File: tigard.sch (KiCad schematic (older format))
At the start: 89 parts, among them J1 USB_C_Receptacle_USB2.0, J2 JTAG, J3 UART, J4 SPI, J5 CORTEX, J6 LA, Q1 BSH103, SW1 TARGET, SW2 MODE, U1 AP7365-18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

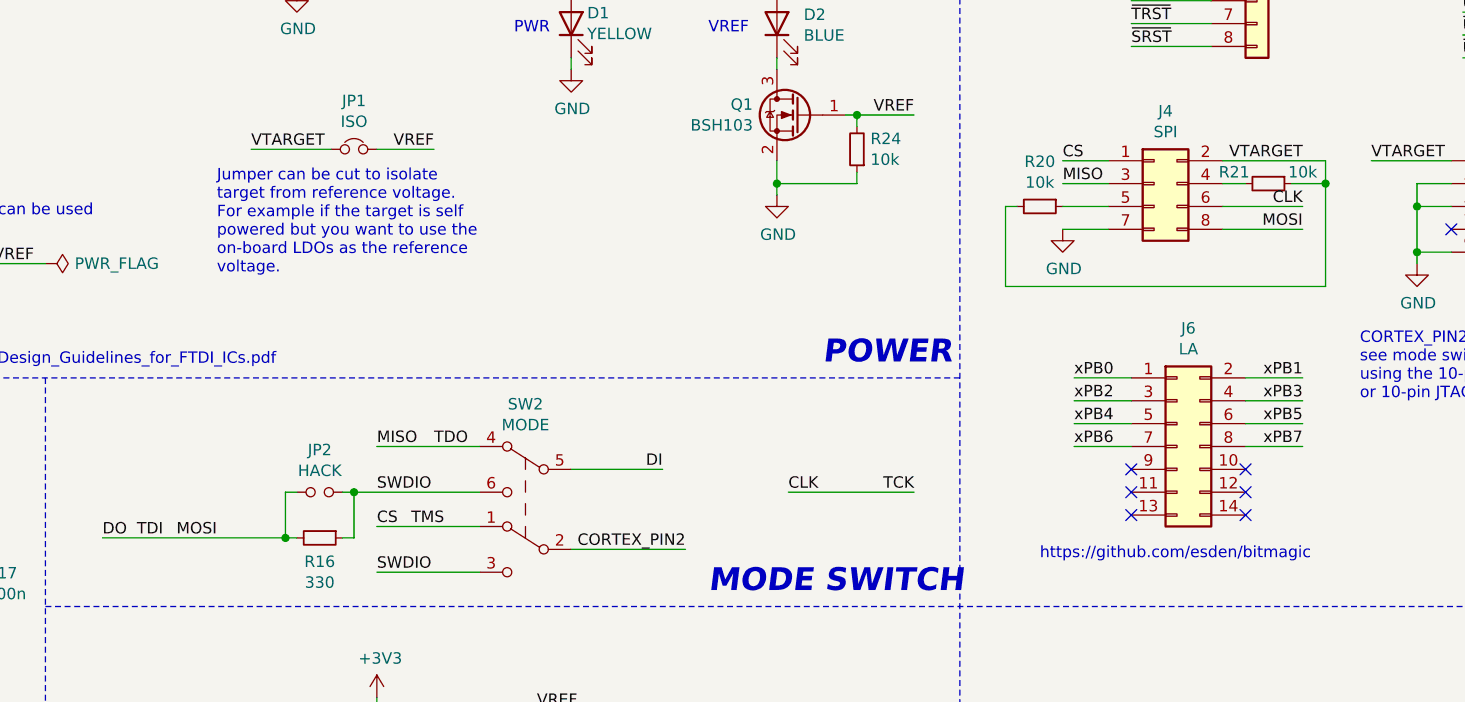
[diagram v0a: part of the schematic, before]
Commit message: Replace all instances of MISO/MOSI with CIPO/COPI
https://www.oshwa.org/a-resolution-to-redefine-spi-signal-names

Closes #12
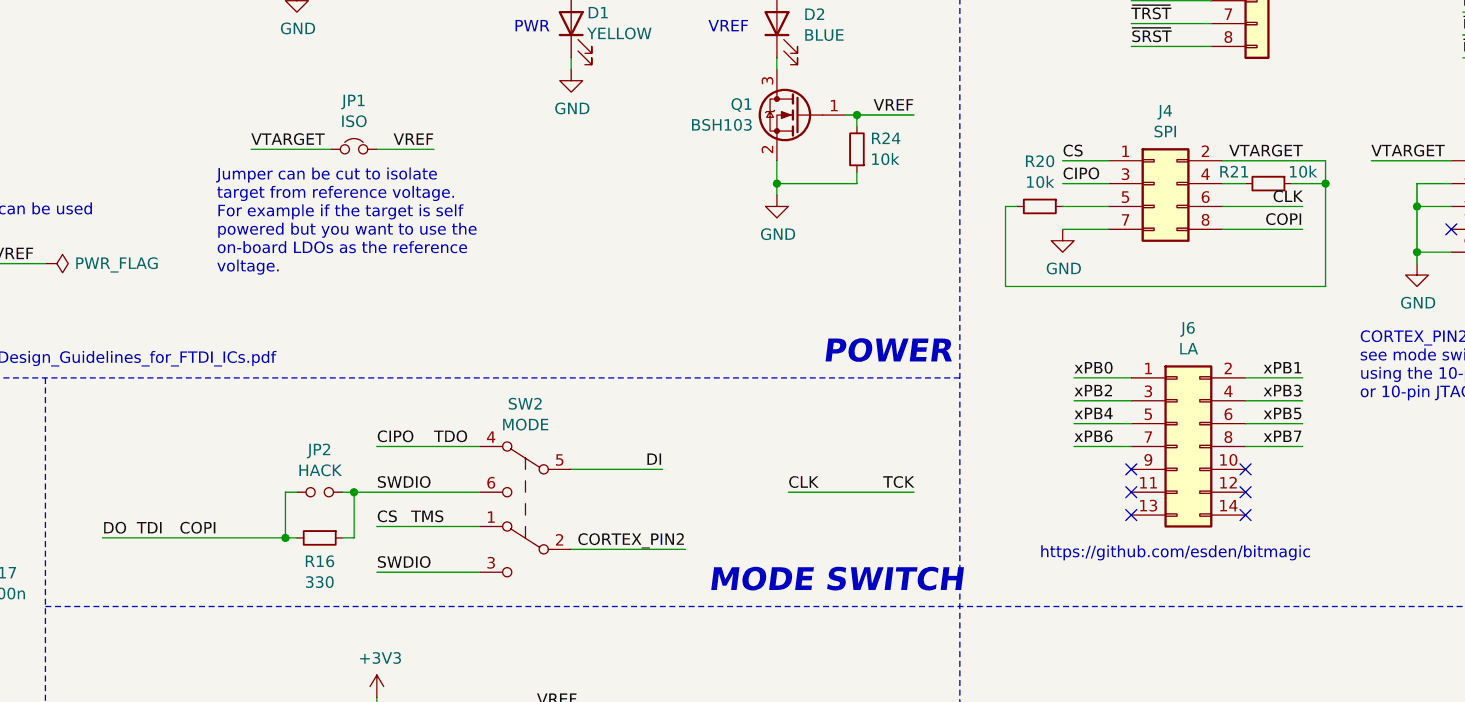
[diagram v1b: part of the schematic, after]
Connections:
- net DO renamed COPI
- net MISO renamed CIPO
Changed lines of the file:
@@
 CS
 Text Label 9250 2200 0    50   ~ 0
-MISO
+CIPO
 $Comp
 L power:GND #PWR0118
@@
 CLK
 Text Label 10300 2400 2    50   ~ 0
-MOSI
+COPI
 NoConn ~ 10950 2400
 Text Label 10600 2100 0    50   ~ 0
@@
 TDO
 Text Label 6250 3350 0    50   ~ 0
-MISO
+CIPO
 Wire Wire Line
 	6250 3350 6700 3350
@@
 TDI
 Text Label 5550 3750 2    50   ~ 0
-MOSI
+COPI
 Text Label 5050 3750 0    50   ~ 0
 DO

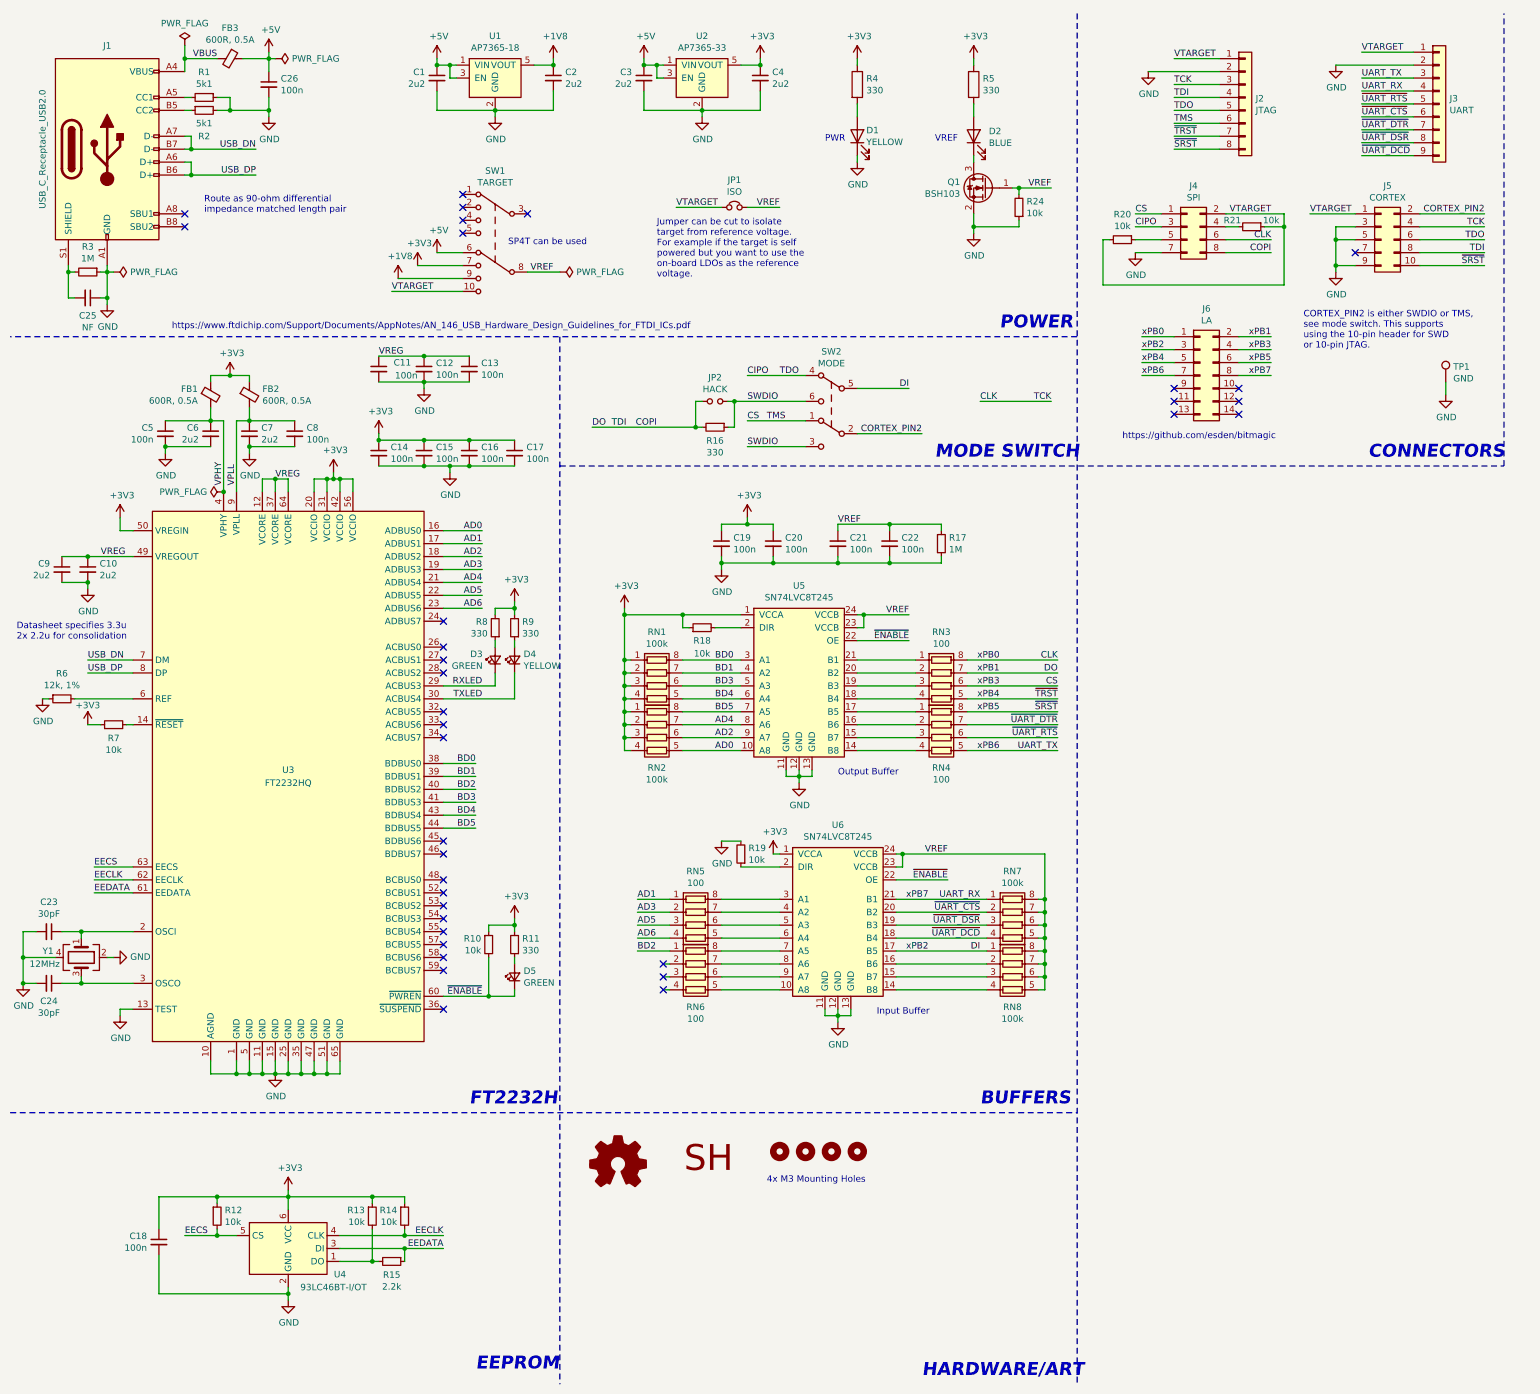
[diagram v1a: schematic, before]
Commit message: Add Qwiic/stemma qt connector (closes #14)
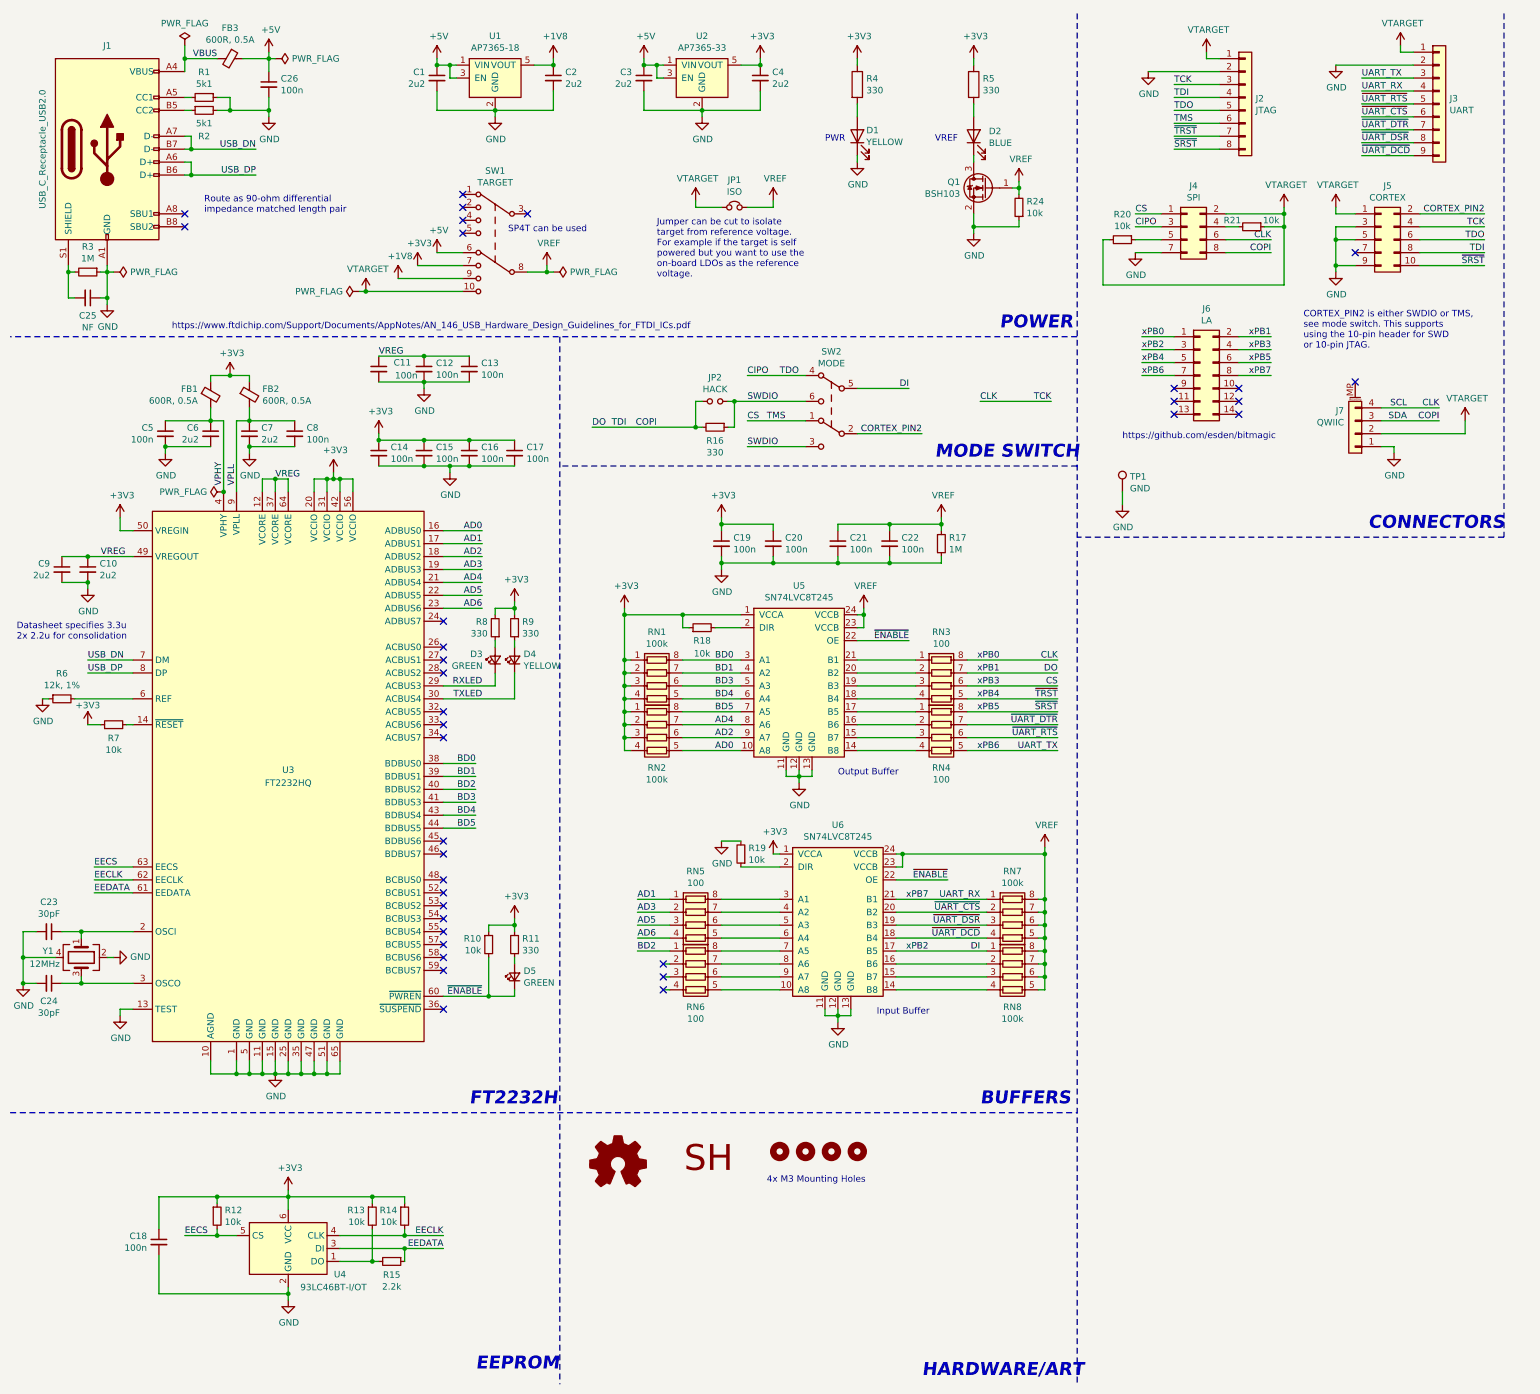
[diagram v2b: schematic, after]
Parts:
- added J7: QWIIC, Connector_JST:JST_SH_SM04B-SRSS-TB_1x04-1MP_P1.00mm_Horizontal, symbol Connector_Generic_MountingPin:Conn_01x04_MountingPin
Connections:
- net CLK: now also J7.4 (Pin_4)
- net COPI: now also J7.3 (Pin_3)
- net GND: now also J7.1 (Pin_1)
- net VTARGET: now also J7.2 (Pin_2)
- no-connect marks 35 -> 36
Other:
- moved on the sheet: TP1

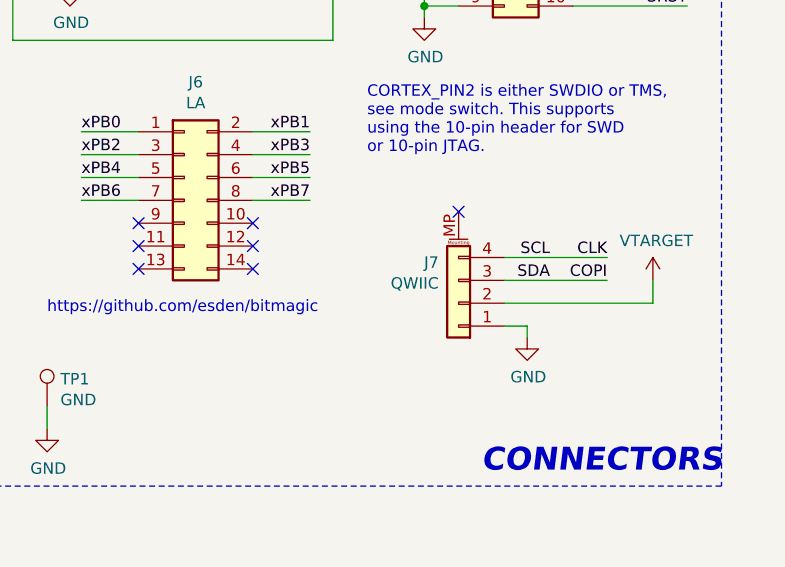
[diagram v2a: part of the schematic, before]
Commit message: Rename QWIIC connector to I2C
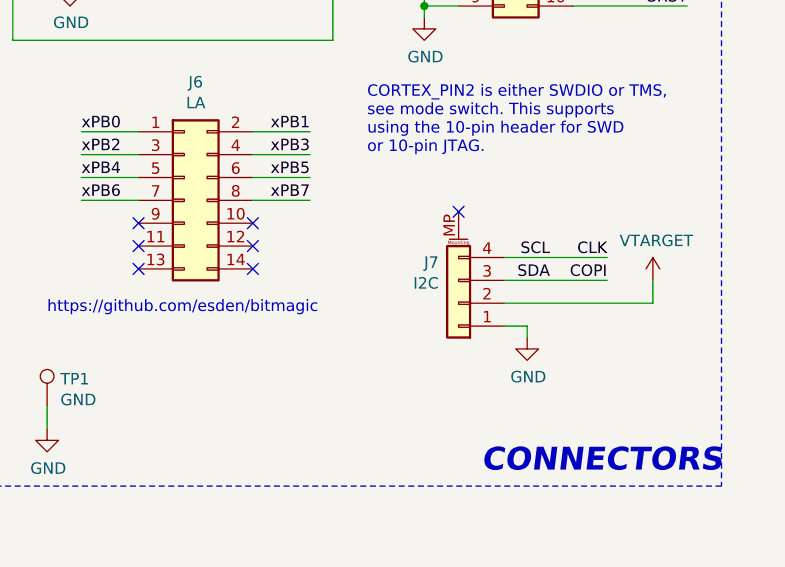
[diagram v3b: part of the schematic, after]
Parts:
- J7: value QWIIC -> I2C
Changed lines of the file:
@@
 P 10950 3800
 F 0 "J7" H 11037 3622 50  0000 L CNN
-F 1 "QWIIC" H 11037 3713 50  0000 L CNN
+F 1 "I2C" H 11037 3713 50  0000 L CNN
 F 2 "Connector_JST:JST_SH_SM04B-SRSS-TB_1x04-1MP_P1.00mm_Horizontal" H 10950 3800 50  0001 C CNN
 F 3 "~" H 10950 3800 50  0001 C CNN

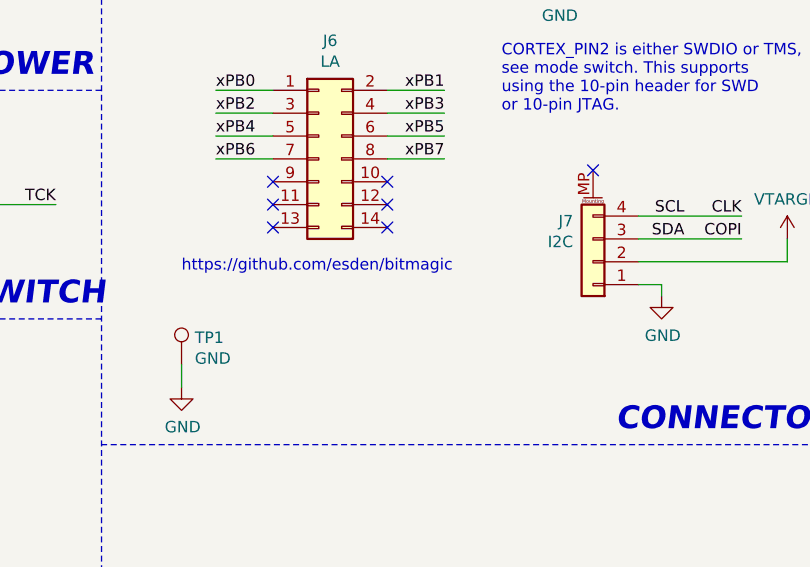
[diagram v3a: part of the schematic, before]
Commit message: Connect LA header to GND (closes #21)
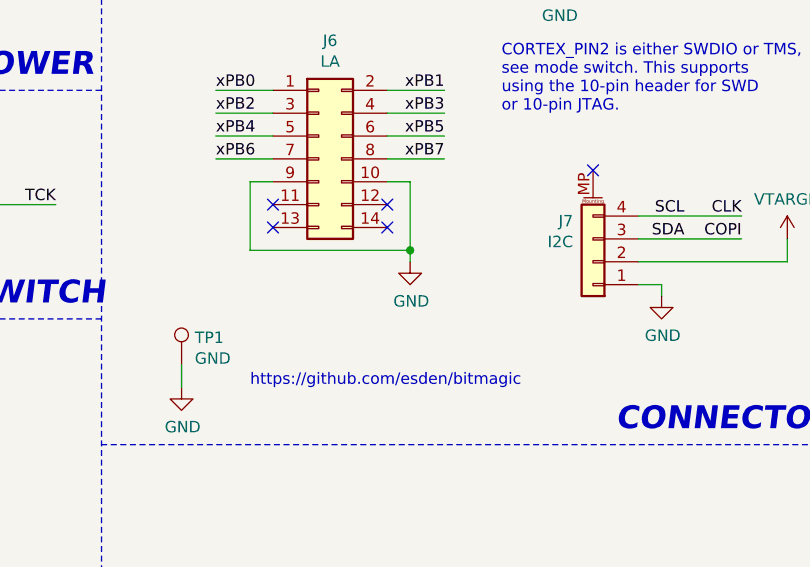
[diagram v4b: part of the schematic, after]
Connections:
- net GND: now also J6.10 (Pin_10), J6.9 (Pin_9)
- no-connect marks 36 -> 34
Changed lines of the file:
@@
 	1    0    0    -1
 $EndComp
-NoConn ~ 9550 3450
 NoConn ~ 9550 3550
 NoConn ~ 9550 3650
 NoConn ~ 10050 3650
 NoConn ~ 10050 3550
-NoConn ~ 10050 3450
 Wire Wire Line
 	1900 800  1900 900
@@
 Text Label 8050 7800 2    50   ~ 0
 DI
-Text Notes 9150 3850 0    50   ~ 0
+Text Notes 9450 4350 0    50   ~ 0
 https://github.com/esden/bitmagic
 $Comp
@@
 	3250 2700 3300 2700
 Connection ~ 3300 2700
+$Comp
+L power:GND #PWR?
+U 1 1 5F303A88
+P 10150 3800
+F 0 "#PWR?" H 10150 3550 50  0001 C CNN
+F 1 "GND" H 10155 3627 50  0000 C CNN
+F 2 "" H 10150 3800 50  0001 C CNN
+F 3 "" H 10150 3800 50  0001 C CNN
+	1    10150 3800
+	1    0    0    -1
+$EndComp
+Wire Wire Line
+	10050 3450 10150 3450
+Wire Wire Line
+	10150 3450 10150 3750
+Wire Wire Line
+	9550 3450 9450 3450
+Wire Wire Line
+	9450 3450 9450 3750
+Wire Wire Line
+	9450 3750 10150 3750
+Connection ~ 10150 3750
+Wire Wire Line
+	10150 3750 10150 3800
 $EndSCHEMATC
